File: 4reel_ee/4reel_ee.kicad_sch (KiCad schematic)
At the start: 26 parts, among them J1 USB_C_Receptacle_USB2.0_16P, J2 Micro_SD_Card_Det2, J3 RJ45_Hanrun_HR911105A_Horizon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, J4 JST, U5 TPD2EUSB30

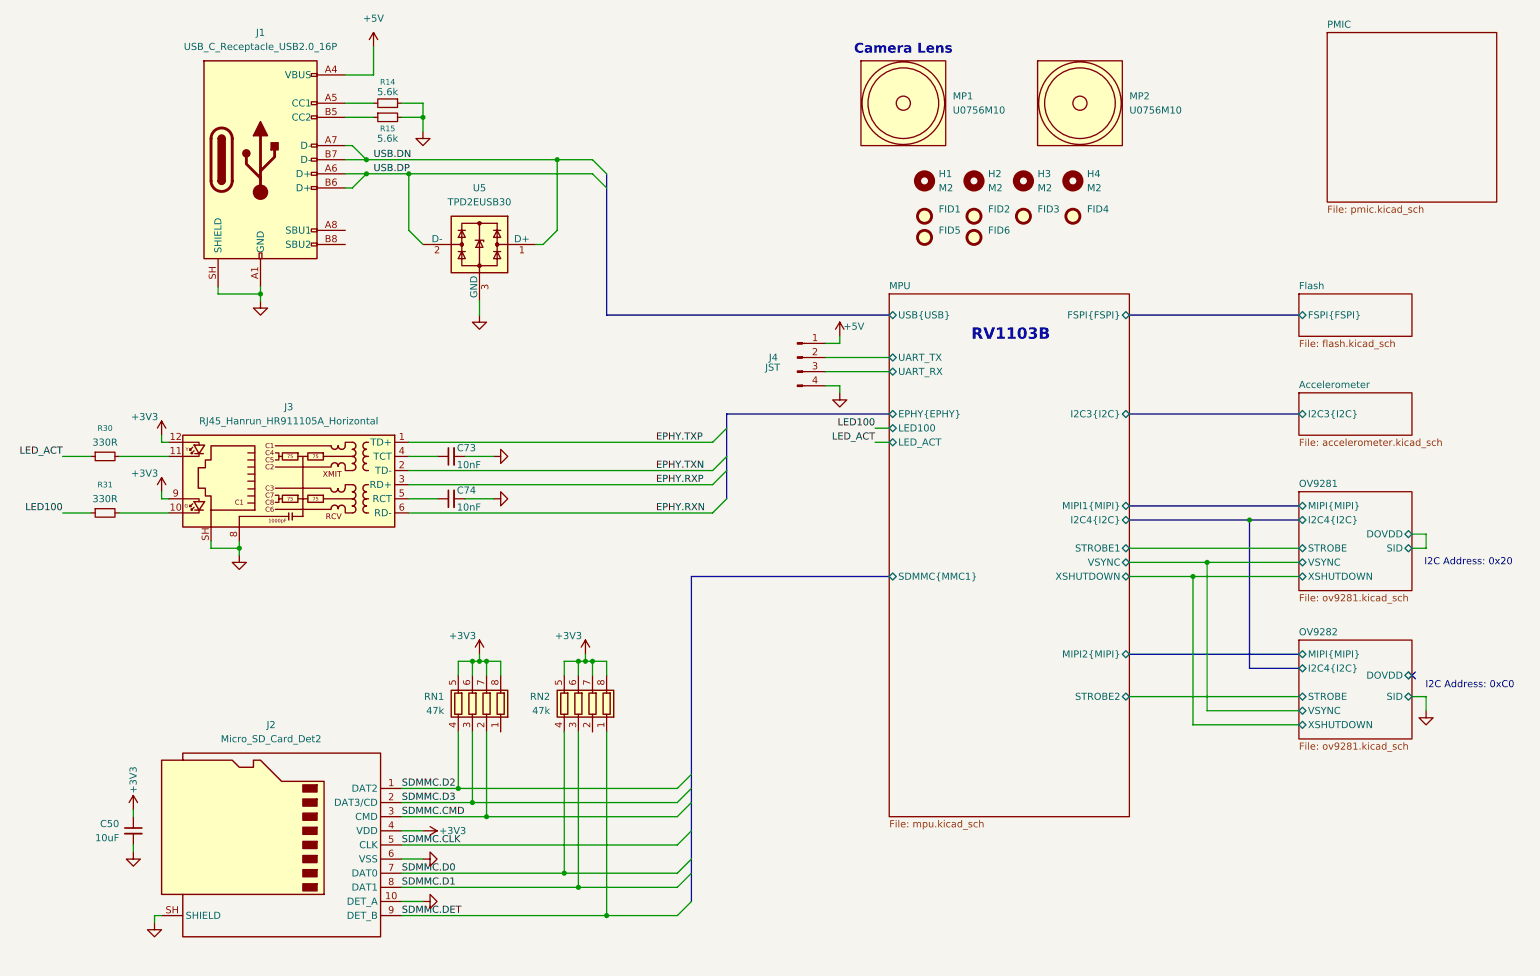
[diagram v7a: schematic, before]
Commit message: Initial schematic, routing finished for RV1106 based design.
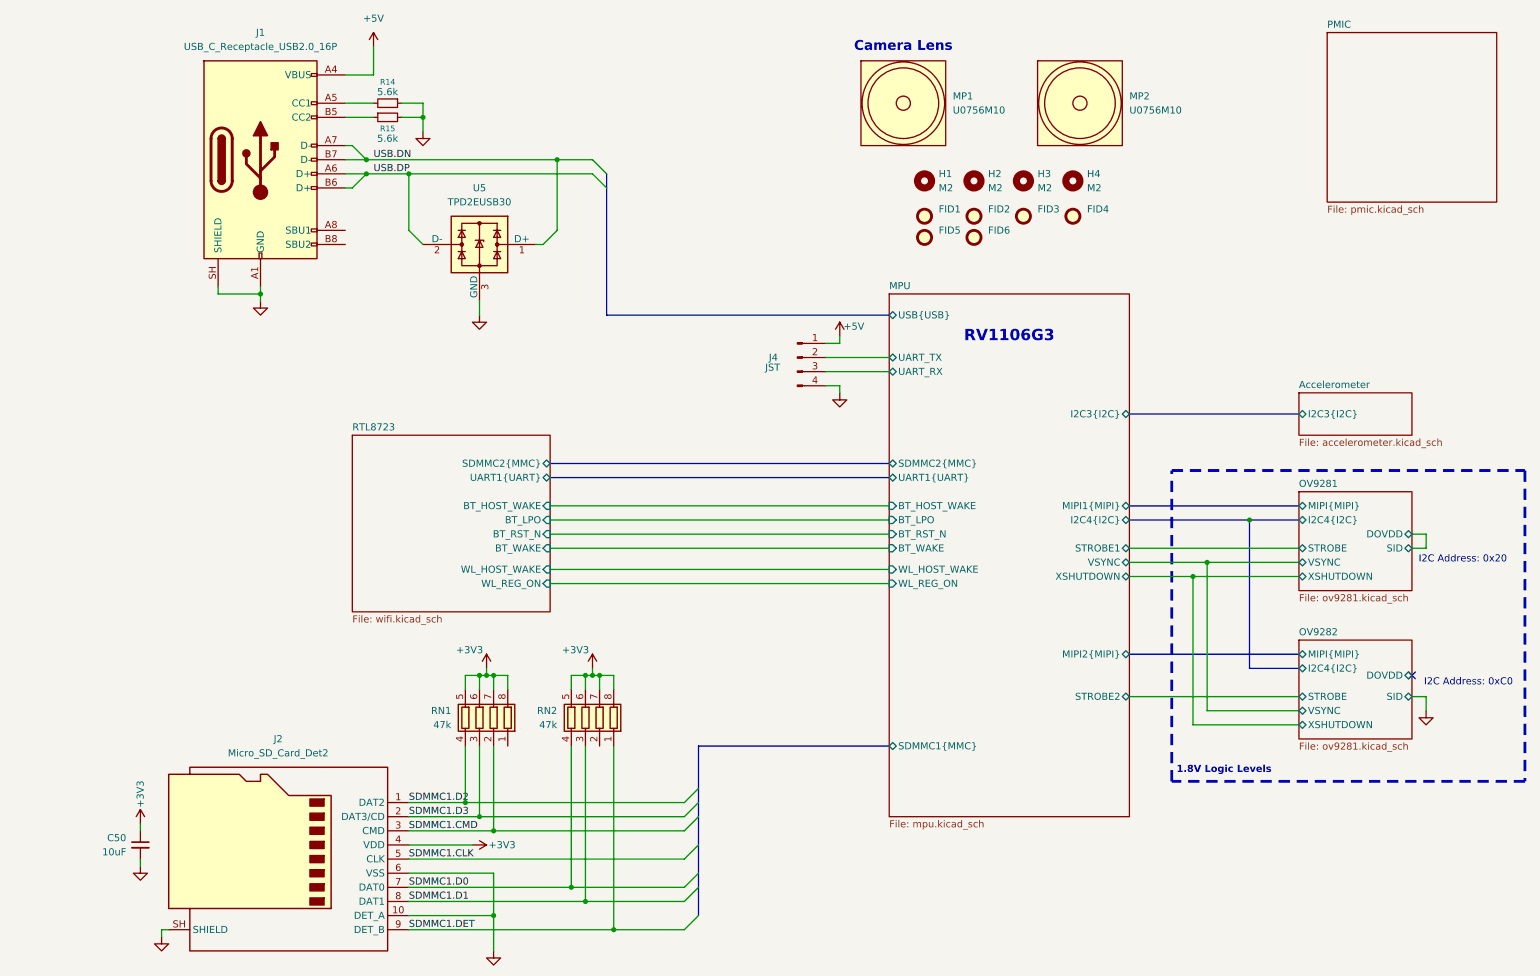
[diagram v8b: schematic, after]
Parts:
- removed C73, C74: 10nF, Capacitor_SMD:C_0402_1005Metric, symbol Device:C_Small
- removed J3: RJ45_Hanrun_HR911105A_Horizontal, Connector_RJ:RJ45_Hanrun_HR911105A_Horizontal, symbol Connector:RJ45_Hanrun_HR911105A_Horizontal
- removed R30, R31: 330R, Resistor_SMD:R_0402_1005Metric, symbol Device:R_Small
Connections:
- net SDMMC.CLK renamed SDMMC1.CLK
- net SDMMC.CMD renamed SDMMC1.CMD
- net SDMMC.D0 renamed SDMMC1.D0
- net SDMMC.D1 renamed SDMMC1.D1
- net SDMMC.D2 renamed SDMMC1.D2
- net SDMMC.D3 renamed SDMMC1.D3
- net SDMMC.DET renamed SDMMC1.DET
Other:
- removed sheet Flash
- added sheet RTL8723 (wifi.kicad_sch)
- sheet MPU ports: added BT_HOST_WAKE, BT_LPO, BT_RST_N, BT_WAKE, SDMMC1{MMC}, SDMMC2{MMC}, UART1{UART}, WL_HOST_WAKE, WL_REG_ON; removed EPHY{EPHY}, FSPI{FSPI}, LED100, LED_ACT, SDMMC{MMC1}
- note added: "1.8V Logic Levels"
- note added: "RV1106G3"
- note removed: "RV1103B"
- moved on the sheet: C50, J2, RN1, RN2
